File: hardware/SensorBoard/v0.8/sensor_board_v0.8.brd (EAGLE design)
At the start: 52.5 x 43 mm, 48 parts, among them IC1 BMP280, J3 USB-MICROB, U10 CCS811, U11 RFM69HW, U2 TSL2561, U3 ATMEGA328P-MU, U5 FT231XS, U7 SHT31, U8 MCP1703/3.3V, U9 MCP1703CB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

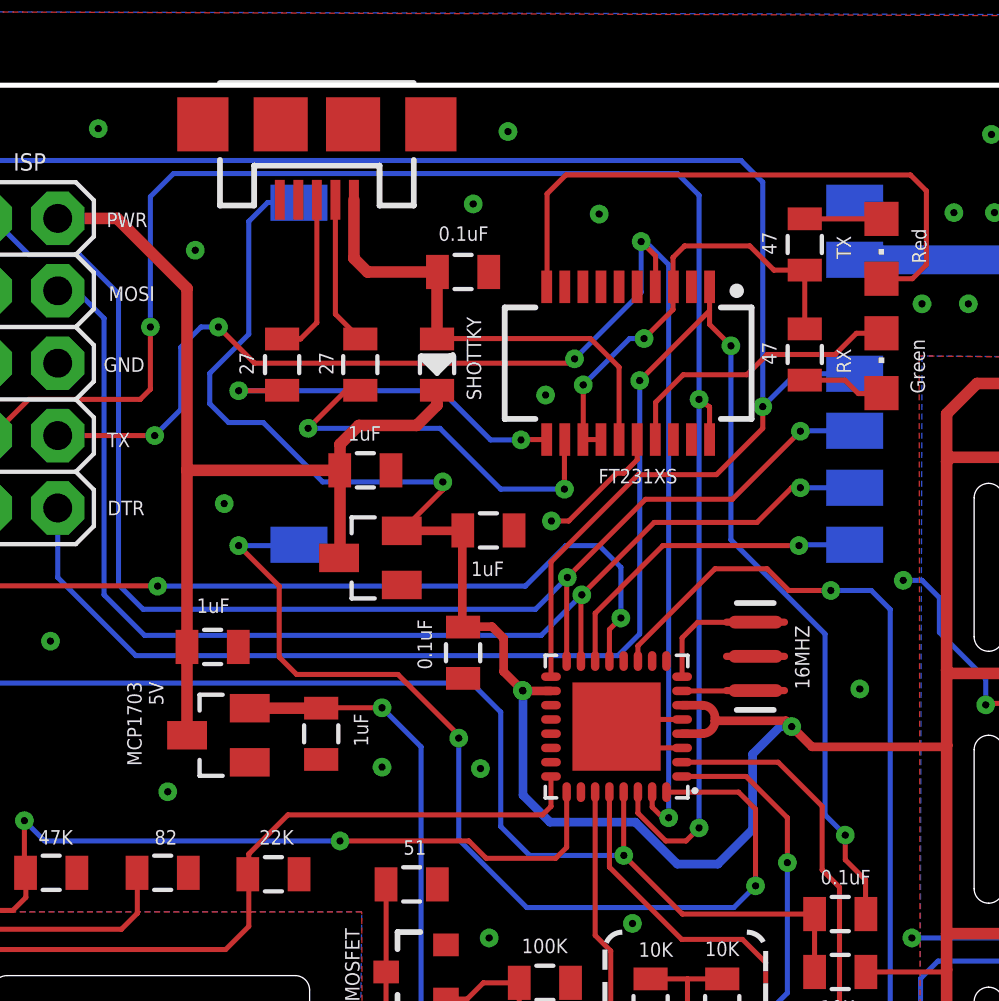
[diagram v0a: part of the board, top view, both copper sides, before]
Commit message: Replaced FT231X SSOP with QFN package
New part number: FT231XQ-R
Adjusted several traces for the new package
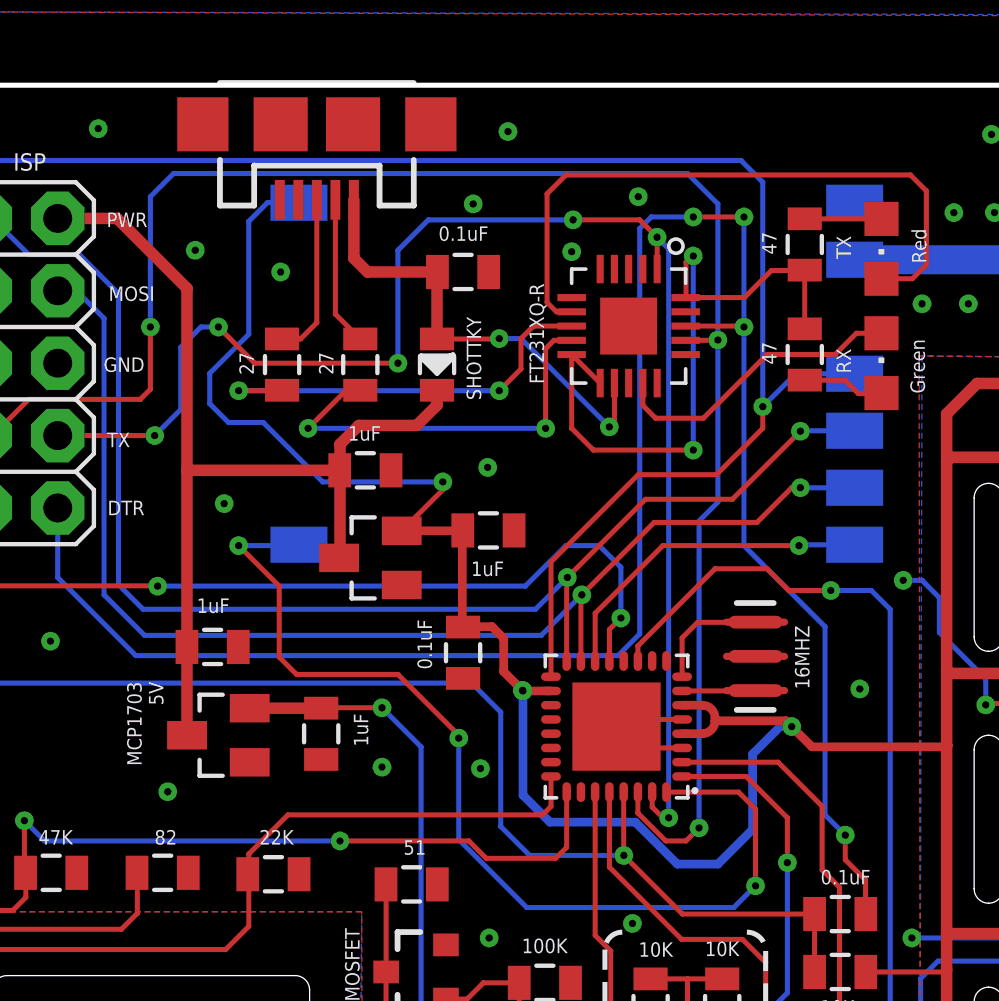
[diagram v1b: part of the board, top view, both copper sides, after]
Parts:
- removed U5: FT231XS, SparkFun-DigitalIC:SSOP20_L
- added U$1: FT231XQ-R, ftdi_ft231xq-r:FTDI_FT231XQ-R_PACKAGE
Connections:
- net DTR: now also U$1.DTR#; no longer U5.1
- net FTDI_VCC: now also U$1.3V3OUT, U$1.RESET#, U$1.VCCIO; no longer U5.13, U5.14, U5.3
- net GND: now also U$1.GND_PIN13, U$1.GND_PIN21, U$1.GND_PIN3; no longer U5.16, U5.6
- net N$17: now also U$1.CBUS1; no longer U5.17
- net N$18: now also U$1.CBUS2; no longer U5.10
- net N$25: now also U$1.USBDM; no longer U5.12
- net N$26: now also U$1.USBDP; no longer U5.11
- net RX: now also U$1.TXD; no longer U5.20
- net TX: now also U$1.RXD; no longer U5.4
- net VBUS: now also U$1.VCC; no longer U5.15
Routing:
- net DTR: track 60.9 -> 70.7 mm, vias 3 -> 4
- net FTDI_VCC: track 15.9 -> 23.6 mm
- net GND: track 66.5 -> 61.9 mm, vias 34 -> 35
- net N$26: track 13.1 -> 14.8 mm
- net TX: track 50.4 -> 52.0 mm, vias 5 -> 6
- net N$18: track 21.5 -> 23.0 mm
- net N$25: track 14.0 -> 14.5 mm
- net VBUS: track 16.9 -> 16.5 mm, vias 0 -> 2
